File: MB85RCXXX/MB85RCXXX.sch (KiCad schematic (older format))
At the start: 15 parts, among them J1 Conn_01x05, U1 MB85RC256V

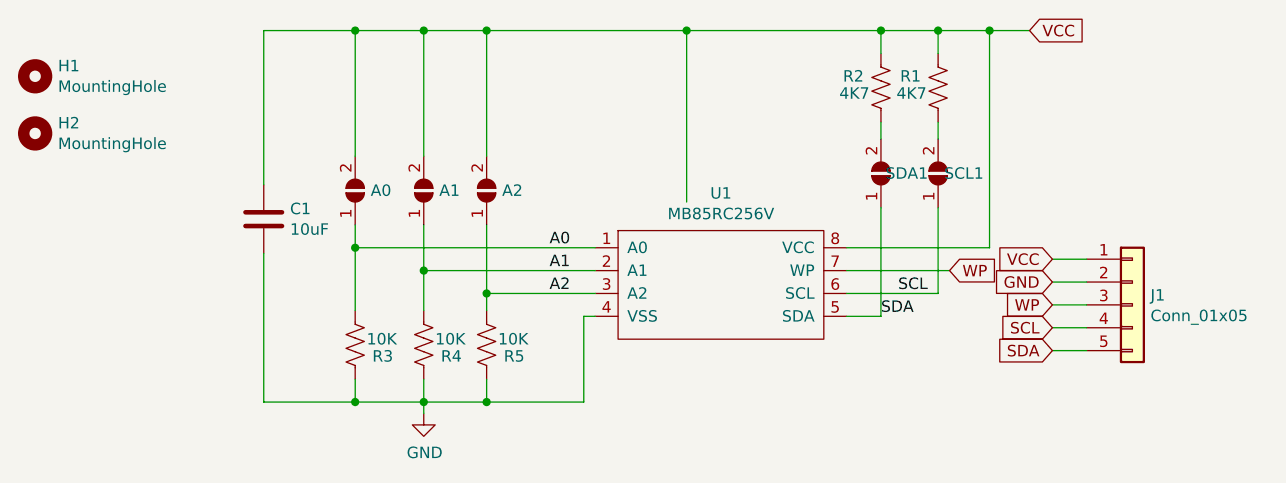
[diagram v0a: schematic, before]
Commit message: MB85RXXX Added in place of MB85RC256V
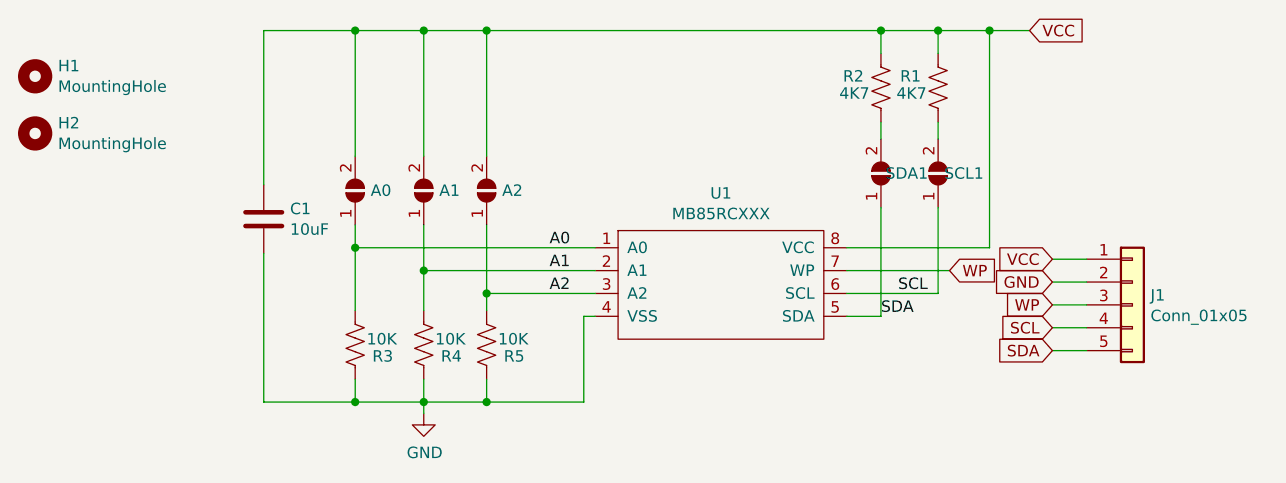
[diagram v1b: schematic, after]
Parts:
- U1: value MB85RC256V -> MB85RCXXX
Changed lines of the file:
@@
 encoding utf-8
 Sheet 1 1
-Title "MB85RC256V Based FRAM Module"
+Title "MB85RCXXX Based FRAM Module"
 Date "2019-12-06"
 Rev "1"
@@
 Comment1 "SirBoard"
 Comment2 "SirKeep"
-Comment3 "MB85RC256V"
+Comment3 "MB85RC64, MB85RC128, MB85RC256, MB85RC512, MB85RC1M"
 Comment4 ""
 $EndDescr
@@
 	1    0    0    -1
 $EndComp
-Wire Wire Line
-	4300 1150 4300 1900
 $Comp
 L Connector_Generic:Conn_01x05 J1
@@
 	3150 2775 3150 2825
 Wire Wire Line
-	4300 1150 3425 1150
-Wire Wire Line
 	2850 1150 2850 1700
-Connection ~ 4300 1150
 Wire Wire Line
 	3150 1700 3150 1150
@@
 P 4450 2300
 F 0 "U1" H 4450 2738 50  0000 C CNN
-F 1 "MB85RC256V" H 4450 2648 50  0000 C CNN
+F 1 "MB85RCXXX" H 4450 2648 50  0000 C CNN
 F 2 "Package_SO:SO-8_3.9x4.9mm_P1.27mm" H 4450 2300 50  0001 C CNN
 F 3 "" H 4450 2300 50  0001 C CNN
@@
 Wire Wire Line
 	5150 1150 5400 1150
-Wire Wire Line
-	4300 1150 5150 1150
 Wire Wire Line
 	5800 1150 5625 1150
@@
 Text Label 5225 2300 0    50   ~ 0
 SCL
+Wire Wire Line
+	3425 1150 5150 1150
 $EndSCHEMATC

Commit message: Schematic PDF and 3D Renders added
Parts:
- U1: symbol MB85RC256V:MB85RC256V -> MB85RCXXX-rescue:MB85RC256V-MB85RC256V
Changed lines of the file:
@@
 EESchema Schematic File Version 4
-LIBS:MB85RC256V-cache
+LIBS:MB85RCXXX-cache
 EELAYER 29 0
 EELAYER END
@@
 VCC
 $Comp
-L MB85RC256V:MB85RC256V U1
+L MB85RCXXX-rescue:MB85RC256V-MB85RC256V U1
 U 1 1 5DEB39FE
 P 4450 2300

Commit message: Part numbers added for all variants
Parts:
- U1: Part C47538 -> C99345; C126727; C47538; C126729; C209975
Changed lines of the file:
@@
 F 2 "Package_SO:SO-8_3.9x4.9mm_P1.27mm" H 4450 2300 50  0001 C CNN
 F 3 "" H 4450 2300 50  0001 C CNN
-F 4 "C47538" H 4450 2300 50  0001 C CNN "Part"
+F 4 "C99345; C126727; C47538; C126729; C209975" H 4450 2300 50  0001 C CNN "Part"
 	1    4450 2300
 	1    0    0    -1
